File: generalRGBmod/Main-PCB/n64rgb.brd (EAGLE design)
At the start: 48.9 x 32.4 mm, 71 parts, among them U1 5M570ZT100C5, U2 THS7374, U3 TLV70018-DDC

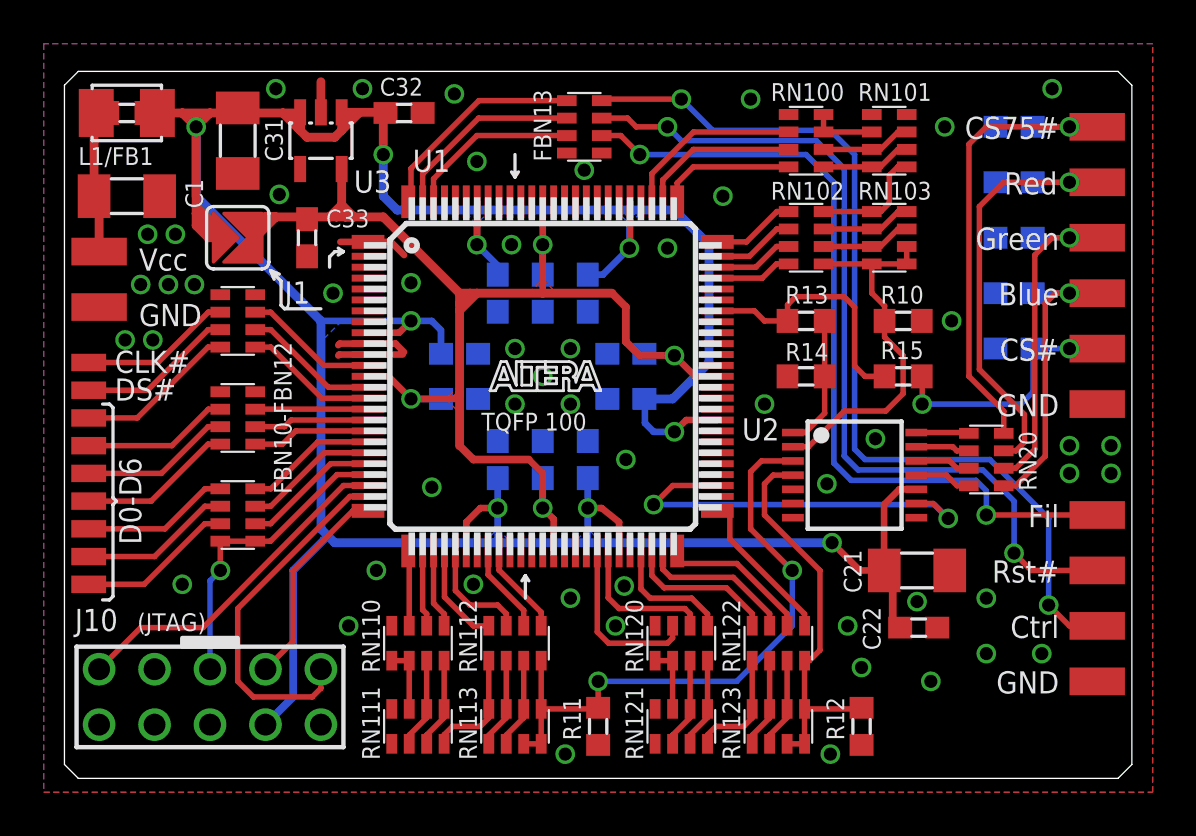
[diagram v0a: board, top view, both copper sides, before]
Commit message: PCB Update: - rotate JTAG header by 180deg - pull-ups and -downs for TCK, TMS and TDI as recommended by Altera / Intel - thicker wire for Vcc near pad
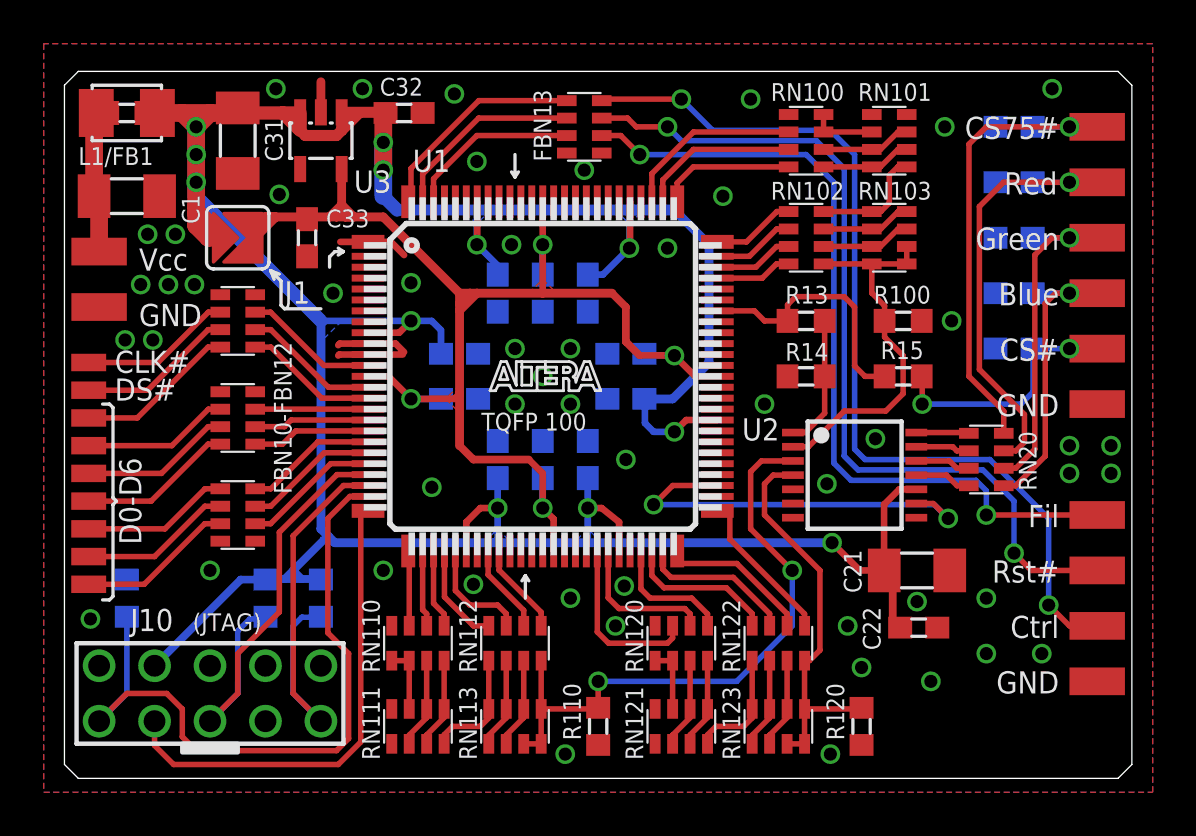
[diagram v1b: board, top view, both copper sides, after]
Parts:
- added R100, R110, R120: 270, rcl:R0603
- R10: value 270 -> 1k
- R11, R12: value 270 -> 10k
- moved R10 37.8 mm to (3.81, 8.89), flipped to the bottom, turned to 270 degrees
- moved R12 25.5 mm to (12.7, 8.89), flipped to the bottom, turned to 270 degrees
- moved R11 16.3 mm to (10.2, 8.89), flipped to the bottom, turned to 270 degrees
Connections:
- net GND: now also R100.1, R110.1, R120.1; no longer R11.1, R12.1
- net N$31: now also R120.2; no longer R12.2
- net N$48: now also R100.2; no longer R10.2
- net N$76: now also R110.2; no longer R11.2
- net TCK: now also R10.2
- net TDI: now also R12.2
- net TMS: now also R11.2; no longer FBN10.4, FBN10.5
- net VCC@3.3V: now also R11.1, R12.1
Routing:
- net TCK: track 16.6 -> 32.1 mm
- net TDO: track 9.61 -> 22.5 mm
- net TMS: track 14.1 -> 21.9 mm, vias 2 -> 1
- net VCC@3.3V: track 159.8 -> 165.0 mm, vias 10 -> 13
- net TDI: track 15.8 -> 20.3 mm
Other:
- board text added: "R100"
- board text added: "R110"
- board text added: "R120"
- board text added: "Vers: N64RGB 5M_20170607"
- board text removed: "Vers: N64RGB 5M_20170419"

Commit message: Selectable installation type: either IGR or Switches
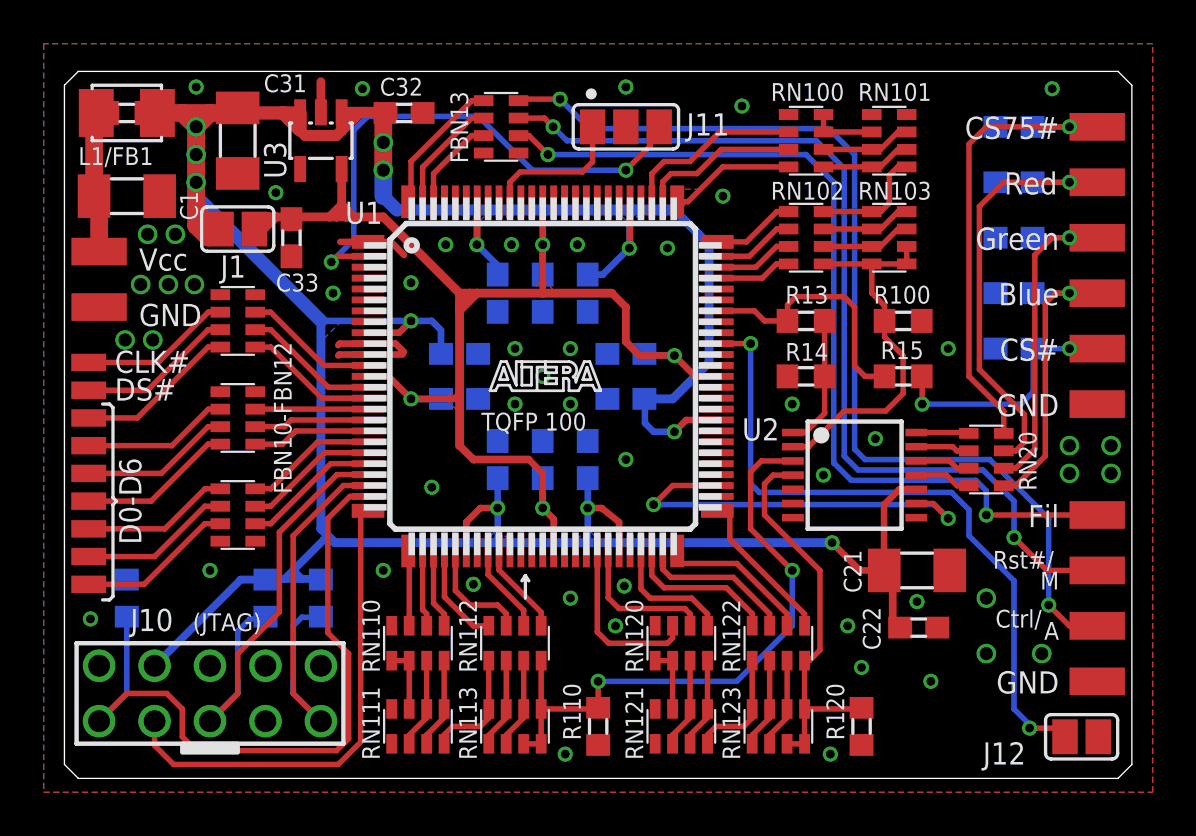
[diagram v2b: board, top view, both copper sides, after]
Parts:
- added J11: (no value), jumper:SJ_2
- added J12: (no value), jumper:SJ
- J1: device snes_div:MYJUMP -> jumper:SJ
- moved FBN13 3.81 mm to (21.0, 30.5)
- moved C33 0.71 mm to (11.4, 25.4)
- moved J1 0.40 mm to (8.89, 25.8)
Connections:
- new net N$49: J12.1, U1.66
- new net N$51: J11.3, U1.91
- new net N$52: J11.1, U1.2
- net CLAMP#: now also U1.68; no longer U1.67
- net GND: now also J11.2, J12.2
- net HSYNC#: now also U1.71; no longer U1.68
- net VCC@1.8V: now also J1.2; no longer J1.P$2
- net VCC@3.3V: now also J1.1; no longer J1.P$1
- net VSYNC#: now also U1.70; no longer U1.66
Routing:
- net N$49: track 0.00 -> 31.4 mm, vias 0 -> 2
- net N$52: track 0.00 -> 24.8 mm, vias 0 -> 2
- net N$51: track 0.00 -> 6.67 mm
- net N$9: track 38.1 -> 41.9 mm
- net N$7: track 42.9 -> 46.8 mm
- net N$47: track 7.97 -> 4.30 mm
- net N$14: track 10.1 -> 6.44 mm
- net N$46: track 8.93 -> 5.31 mm
- net N$8: track 40.4 -> 43.8 mm
- net R2: track 6.27 -> 5.77 mm
- net GND: vias 54 -> 53
- added copper zone on layer 1, net R2
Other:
- board text added: "A"
- board text added: "Ctrl/"
- board text added: "Design is based on the schematics by viletim (for EPM240T100C5) Redesign by borti4938"
- board text added: "J11"
- board text added: "J12"
- board text added: "M"
- board text added: "Rst#/"
- board text added: "Vers: N64RGB 5M_20170901"
- board text added: "__/)__/)_"
- board text removed: "Ctrl"
- board text removed: "Design is based on the schematics by viletim (for EPM240T100C5)"
- board text removed: "Rst#"
- board text removed: "Vers: N64RGB 5M_20170607"
- board text removed: "borti4938 __/)__/)_"

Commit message: change load resistor values at R2R output to have a more colourful picture
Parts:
- R100, R110, R120: value 270 -> 280
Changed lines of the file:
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@@
 <?xml version="1.0" encoding="utf-8"?>
 <!DOCTYPE eagle SYSTEM "eagle.dtd">
-<eagle version="7.7.0">
+<eagle version="8.4.3">
 <drawing>
 <settings>
 <setting alwaysvectorfont="no"/>
+<setting keepoldvectorfont="yes"/>
 <setting verticaltext="up"/>
 </settings>
@@
 <param name="dpMaxLengthDifference" value="10mm"/>
 <param name="dpGapFactor" value="2.5"/>
-<param name="checkGrid" value="0"/>
 <param name="checkAngle" value="0"/>
 <param name="checkFont" value="1"/>
 <param name="checkRestrict" value="0"/>
+<param name="checkStop" value="0"/>
 <param name="useDiameter" value="13"/>
 <param name="maxErrors" value="50"/>
@@
 </element>
 <element name="R15" library="rcl" package="R0603" value="330" x="39.37" y="19.05" smashed="yes"/>
-<element name="R100" library="rcl" package="R0603" value="270" x="39.37" y="21.59" smashed="yes" rot="R180"/>
+<element name="R100" library="rcl" package="R0603" value="280" x="39.37" y="21.59" smashed="yes" rot="R180"/>
 <element name="R13" library="rcl" package="R0603" value="4k7" x="34.925" y="21.59" smashed="yes"/>
 <element name="R14" library="rcl" package="R0603" value="475" x="34.925" y="19.05" smashed="yes"/>
@@
 <attribute name="OC_NEWARK" value="unknown" x="21.59" y="3.01625" size="1.778" layer="27" rot="R180" display="off"/>
 </element>
-<element name="R110" library="rcl" package="R0603" value="270" x="25.4" y="3.01625" smashed="yes" rot="R90"/>
+<element name="R110" library="rcl" package="R0603" value="280" x="25.4" y="3.01625" smashed="yes" rot="R90"/>
 <element name="RN120" library="resistor-net" package="CTS742C083" value="CAT16-2001F4LF " x="29.21" y="6.82625" smashed="yes" rot="R180">
 <attribute name="MF" value="" x="29.21" y="6.82625" size="1.778" layer="27" rot="R180" display="off"/>
@@
 <attribute name="OC_NEWARK" value="unknown" x="33.655" y="3.01625" size="1.778" layer="27" rot="R180" display="off"/>
 </element>
-<element name="R120" library="rcl" package="R0603" value="270" x="37.465" y="3.01625" smashed="yes" rot="R90"/>
+<element name="R120" library="rcl" package="R0603" value="280" x="37.465" y="3.01625" smashed="yes" rot="R90"/>
 <element name="DSYNC#" library="wirepad" package="SMD0,8-1,6" value="" x="2.06375" y="18.415" smashed="yes" rot="R90"/>
 <element name="CLOCK#" library="wirepad" package="SMD0,8-1,6" value="" x="2.06375" y="19.685" smashed="yes" rot="R90"/>

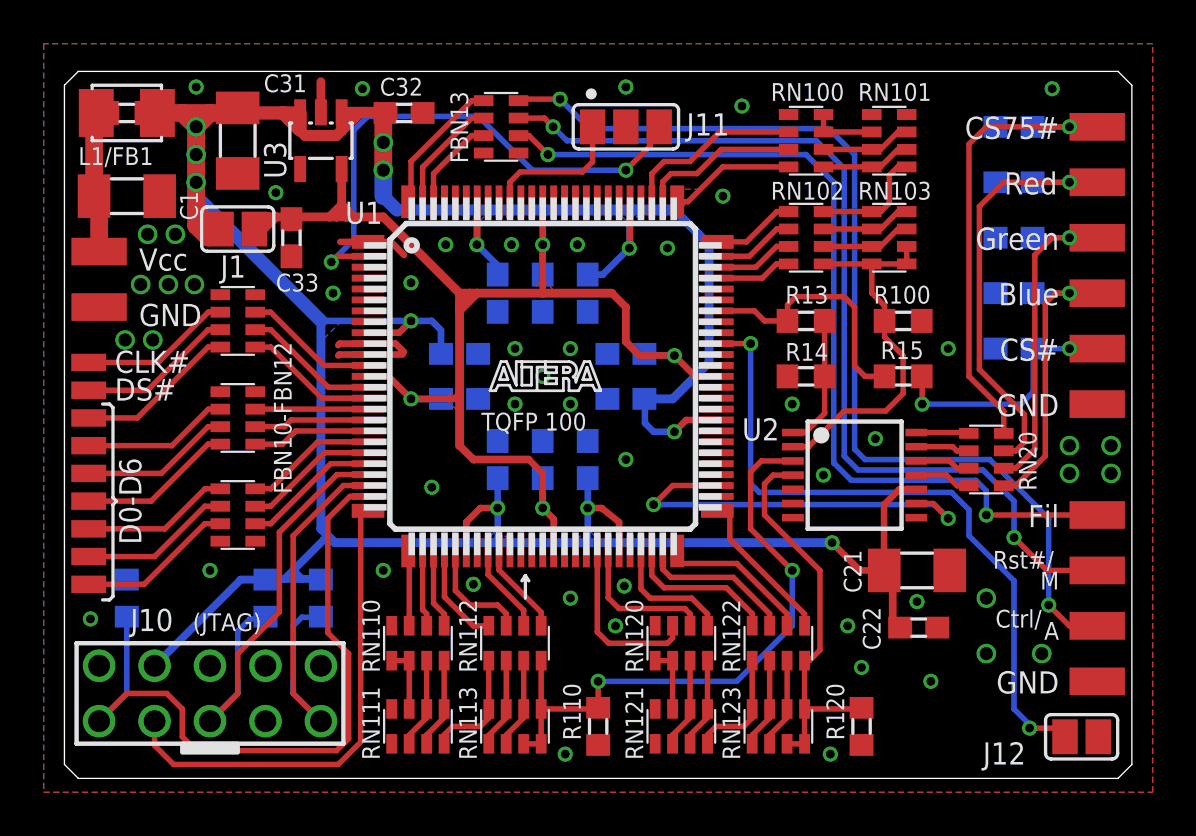
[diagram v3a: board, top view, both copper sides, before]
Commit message: Update PCB: add logo, new name, stencil reduce pad size by 10%
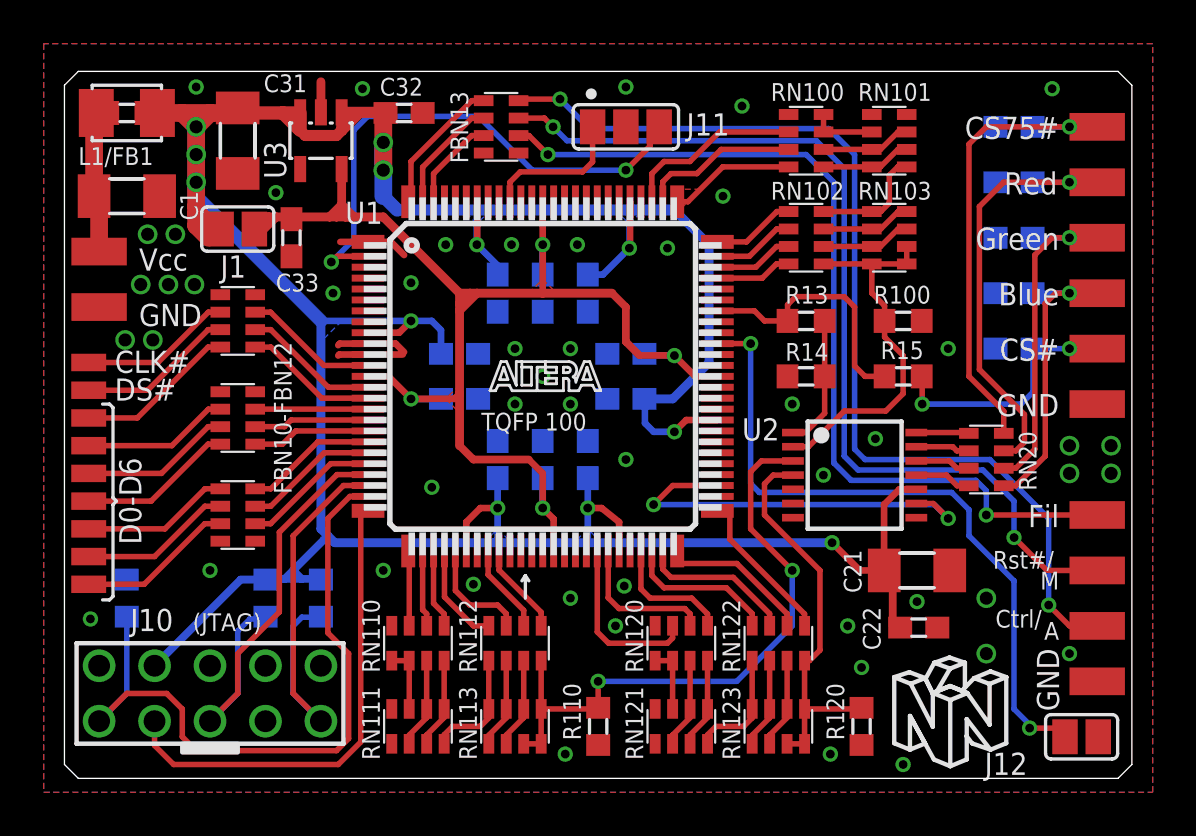
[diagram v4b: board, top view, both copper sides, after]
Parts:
- CLOCK#, D0, D1, D2, D3, D4, D5, D6, DSYNC#: value (none) -> SMD1
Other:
- board text added: "Vers: N64RGBv1 5M_20171211"
- board text removed: "Vers: N64RGB 5M_20170901"
